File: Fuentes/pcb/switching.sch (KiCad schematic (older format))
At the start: 25 parts, among them P1 Vcc, P2 V-switching, P3 V+switching, P4 gnd_switching, P5 Gnd_primario, Q1 MOS_N

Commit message: placa conmutada algunas  pistas
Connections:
- net GND: now also C3.2, C4.1, P4.1 (W), R9.2, nucleo1.4 (GND_Secundario), nucleo1.5 (GND_secundario_2)
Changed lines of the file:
@@
-EESchema Schematic File Version 2  date mar 26 jun 2012 23:30:51 ART
+EESchema Schematic File Version 2  date jue 28 jun 2012 01:18:07 ART
 LIBS:power
 LIBS:device
@@
 Sheet 1 1
 Title ""
-Date "27 jun 2012"
+Date "28 jun 2012"
 Rev ""
 Comp ""
@@
 Comment4 ""
 $EndDescr
-Connection ~ 5400 4650
-Connection ~ 6950 2400
+Connection ~ 8850 2400
+Connection ~ 5600 4650
 Wire Wire Line
-	6950 2450 6950 2300
+	8850 4650 5300 4650
 Wire Wire Line
-	1400 4100 1250 4100
+	8850 4650 8850 2400
+Connection ~ 1500 4100
 Wire Wire Line
-	1300 4100 1500 4100
-Connection ~ 4800 4150
+	4800 4900 4800 4150
+Connection ~ 5550 3750
 Wire Wire Line
-	5000 4150 4800 4150
+	5550 2800 5550 3750
+Wire Wire Line
+	5300 4650 5300 4350
+Wire Wire Line
+	4800 4900 3900 4900
+Connection ~ 5550 2050
+Connection ~ 3900 5300
+Connection ~ 4650 4900
+Wire Wire Line
+	4650 4600 4650 5600
+Connection ~ 2100 4100
+Connection ~ 2100 5100
+Wire Wire Line
+	2100 5200 2100 4700
+Wire Wire Line
+	2100 5200 1900 5200
+Wire Wire Line
+	2600 4500 1750 4500
+Connection ~ 1250 4500
+Wire Wire Line
+	1250 4750 1250 4100
+Connection ~ 1750 4500
+Wire Wire Line
+	1750 4500 1750 4750
+Wire Wire Line
+	1750 4750 1700 4750
+Connection ~ 1400 4100
+Connection ~ 2100 4900
+Wire Wire Line
+	2100 5100 2600 5100
+Connection ~ 2450 4100
+Wire Wire Line
+	2450 4100 2450 3200
+Wire Wire Line
+	2600 3900 2600 3550
+Wire Wire Line
+	2600 3550 10050 3550
+Wire Wire Line
+	3900 4300 4050 4300
+Connection ~ 4400 3950
+Wire Wire Line
+	4400 3950 4650 3950
+Wire Wire Line
+	4650 5600 2600 5600
+Wire Wire Line
+	2600 5600 2600 5300
+Connection ~ 4400 2050
+Wire Wire Line
+	4400 2050 4400 4000
+Connection ~ 9150 1900
+Connection ~ 9150 2400
+Connection ~ 3900 3550
+Wire Wire Line
+	10050 3550 10050 1900
+Wire Wire Line
+	10050 1900 9150 1900
+Wire Wire Line
+	3900 5400 3900 5100
+Wire Wire Line
+	6950 2400 9150 2400
+Wire Wire Line
+	7400 2350 7400 2450
+Connection ~ 7400 2400
+Wire Wire Line
+	7400 1950 7400 1900
+Connection ~ 7400 1900
+Wire Wire Line
+	7400 2850 7400 2900
+Connection ~ 7400 2900
+Wire Wire Line
+	8200 2900 7350 2900
+Wire Wire Line
+	8250 1900 7350 1900
+Wire Wire Line
+	9150 1400 8200 1400
+Wire Wire Line
+	8200 1400 8200 1900
+Connection ~ 8200 1900
+Wire Wire Line
+	3900 4700 4400 4700
+Wire Wire Line
+	4400 4700 4400 4500
+Wire Wire Line
+	3900 4100 4050 4100
+Wire Wire Line
+	4050 4100 4050 3200
+Wire Wire Line
+	4050 3200 2450 3200
+Wire Wire Line
+	2600 4100 2000 4100
+Wire Wire Line
+	3900 3900 3900 3550
+Wire Wire Line
+	2100 4700 2200 4700
+Wire Wire Line
+	4650 3950 4650 4100
+Wire Wire Line
+	1250 4750 1300 4750
+Connection ~ 1900 4500
+Wire Wire Line
+	1900 4700 1900 4500
+Wire Wire Line
+	2100 4100 2100 4300
+Connection ~ 4800 4900
+Wire Wire Line
+	5300 3950 5300 3750
+Wire Wire Line
+	5300 3750 5600 3750
 Wire Wire Line
 	5550 2050 4150 2050
 Wire Wire Line
-	5600 3750 5300 3750
+	4800 4150 5000 4150
+Connection ~ 4800 4150
 Wire Wire Line
-	5300 3750 5300 3950
-Connection ~ 4800 4900
+	1300 4100 1500 4100
 Wire Wire Line
-	2100 4100 2100 4300
+	1250 4100 1400 4100
 Wire Wire Line
-	1900 4700 1900 4500
-Connection ~ 1900 4500
-Wire Wire Line
-	1300 4750 1250 4750
-Wire Wire Line
-	4650 4100 4650 3950
-Wire Wire Line
-	2200 4700 2100 4700
-Wire Wire Line
-	3900 3900 3900 3550
-Wire Wire Line
-	2600 4100 2000 4100
-Wire Wire Line
-	4050 3200 2450 3200
-Wire Wire Line
-	4050 3200 4050 4100
-Wire Wire Line
-	4050 4100 3900 4100
-Wire Wire Line
-	4400 4500 4400 4700
-Wire Wire Line
-	4400 4700 3900 4700
-Connection ~ 8200 1900
-Wire Wire Line
-	8200 1900 8200 1400
-Wire Wire Line
-	8200 1400 9150 1400
-Wire Wire Line
-	8250 1900 7350 1900
-Wire Wire Line
-	8200 2900 7350 2900
-Connection ~ 7400 2900
-Wire Wire Line
-	7400 2850 7400 2900
-Connection ~ 7400 1900
-Wire Wire Line
-	7400 1950 7400 1900
-Connection ~ 7400 2400
-Wire Wire Line
-	7400 2350 7400 2450
-Wire Wire Line
-	6950 2400 9150 2400
-Wire Wire Line
-	3900 5400 3900 5100
-Wire Wire Line
-	9150 1900 10050 1900
-Wire Wire Line
-	10050 1900 10050 3550
-Connection ~ 3900 3550
-Connection ~ 9150 2400
-Connection ~ 9150 1900
-Wire Wire Line
-	4400 2050 4400 4000
-Connection ~ 4400 2050
-Wire Wire Line
-	2600 5300 2600 5600
-Wire Wire Line
-	2600 5600 4650 5600
-Wire Wire Line
-	4650 3950 4400 3950
-Connection ~ 4400 3950
-Wire Wire Line
-	3900 4300 4050 4300
-Wire Wire Line
-	10050 3550 2600 3550
-Wire Wire Line
-	2600 3550 2600 3900
-Wire Wire Line
-	2450 3200 2450 4100
-Connection ~ 2450 4100
-Wire Wire Line
-	2100 5100 2600 5100
-Connection ~ 2100 4900
-Connection ~ 1400 4100
-Wire Wire Line
-	1700 4750 1750 4750
-Wire Wire Line
-	1750 4750 1750 4500
-Connection ~ 1750 4500
-Wire Wire Line
-	1250 4750 1250 4100
-Connection ~ 1250 4500
-Wire Wire Line
-	1750 4500 2600 4500
-Wire Wire Line
-	1900 5200 2100 5200
-Wire Wire Line
-	2100 5200 2100 4700
-Connection ~ 2100 5100
-Connection ~ 2100 4100
-Wire Wire Line
-	4650 5600 4650 4600
-Connection ~ 4650 4900
-Connection ~ 3900 5300
-Connection ~ 5550 2050
-Wire Wire Line
-	3900 4900 4800 4900
-Wire Wire Line
-	5300 4350 5300 4650
-Wire Wire Line
-	5300 4650 5600 4650
-Wire Wire Line
-	5550 2800 5550 3750
-Connection ~ 5550 3750
-Wire Wire Line
-	4800 4900 4800 4150
-Connection ~ 1500 4100
+	6950 2450 6950 2300
+Connection ~ 6950 2400
+Connection ~ 5400 4650
 $Comp
 L CONNECTOR P5

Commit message: 
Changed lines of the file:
@@
-EESchema Schematic File Version 2  date jue 28 jun 2012 01:18:07 ART
+EESchema Schematic File Version 2  date 28/06/2012 03:58:31 p.m.
 LIBS:power
 LIBS:device
@@
 LIBS:nucleo
 LIBS:lm494
-LIBS:switching-cache
+LIBS:sonic
 EELAYER 25  0
 EELAYER END
@@
 Comment4 ""
 $EndDescr
+$Comp
+L LOGO #G1
+U 1 1 4FECA926
+P 6250 5100
+F 0 "#G1" H 6250 4837 60  0001 C CNN
+F 1 "LOGO" H 6250 5363 60  0001 C CNN
+	1    6250 5100
+	1    0    0    -1
+$EndComp
 Connection ~ 8850 2400
 Connection ~ 5600 4650

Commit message: nueva switching beta
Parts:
- added C6: C, symbol C
- added F1: RELE, symbol RELE
- added Q2: NPN, symbol NPN
- added R11, R12, R13: R, symbol R
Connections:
- net GND: now also C6.2, Q2.1 (E), R12.1
- net at P1.1 (W), R6.2, R7.1: now also F1.2 (bobina2), F1.3 (cm), R11.2; no longer nucleo1.1 (V+Primario)
- new net: F1.4 (nc), nucleo1.1 (V+Primario)
- new net: F1.1 (bobina1), R13.1
- new net: C6.1, Q2.2 (B), R11.1, R12.2
- new net: Q2.3 (C), R13.2
- no-connect marks 0 -> 1
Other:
- moved on the sheet: C1, C2, C3, C4, C5, D1, D2, P1, P2, P3, P4, P5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

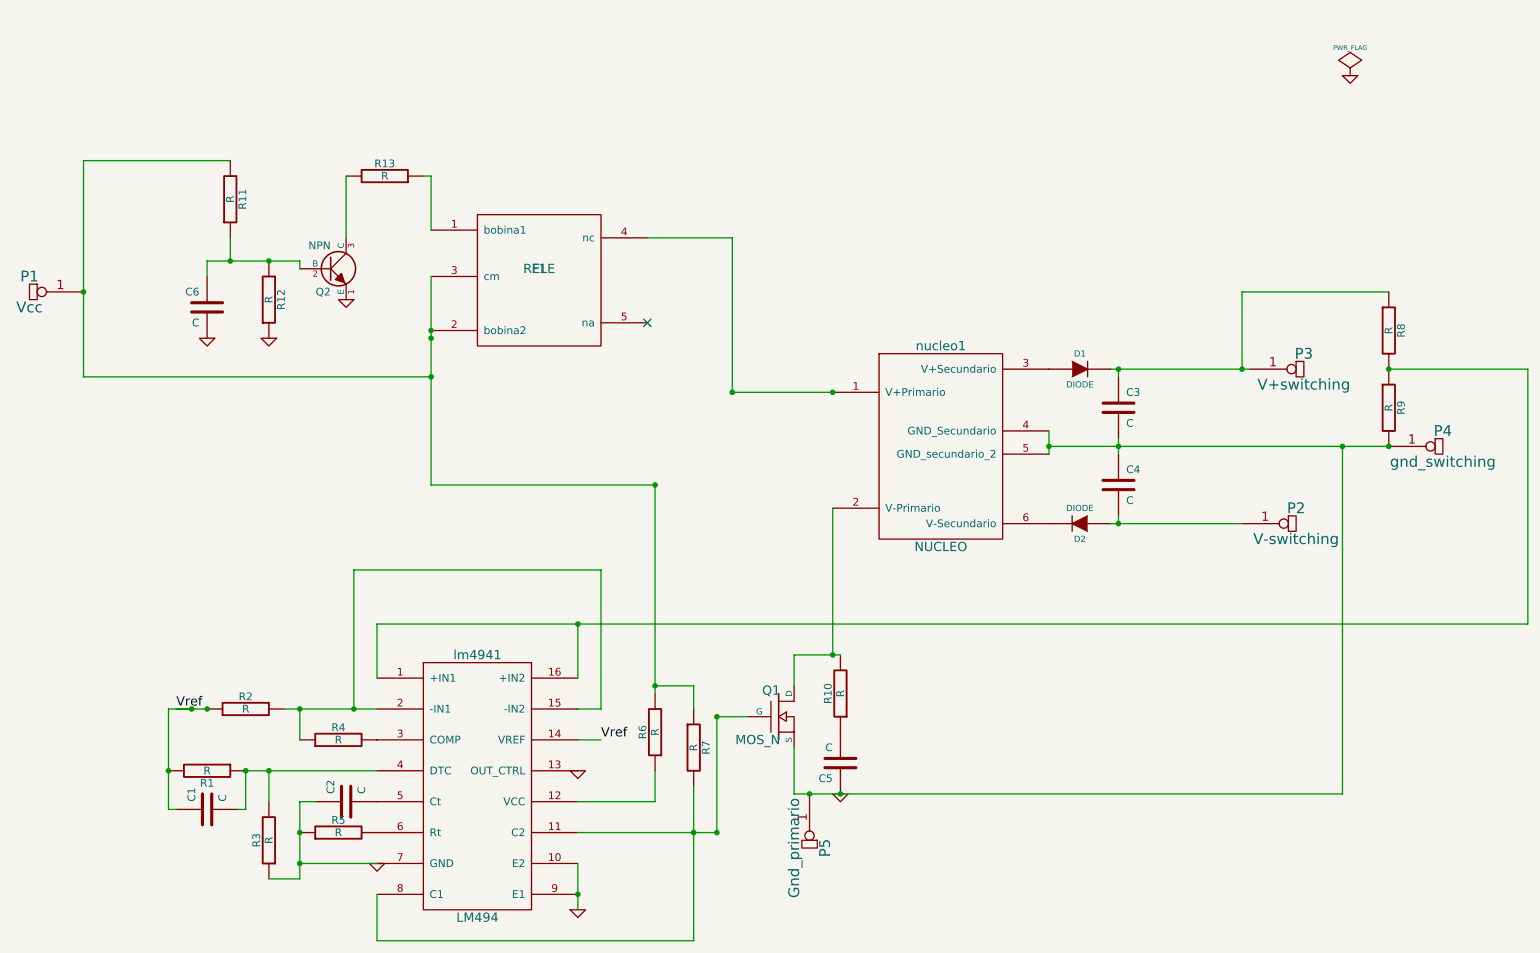
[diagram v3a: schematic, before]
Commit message: 
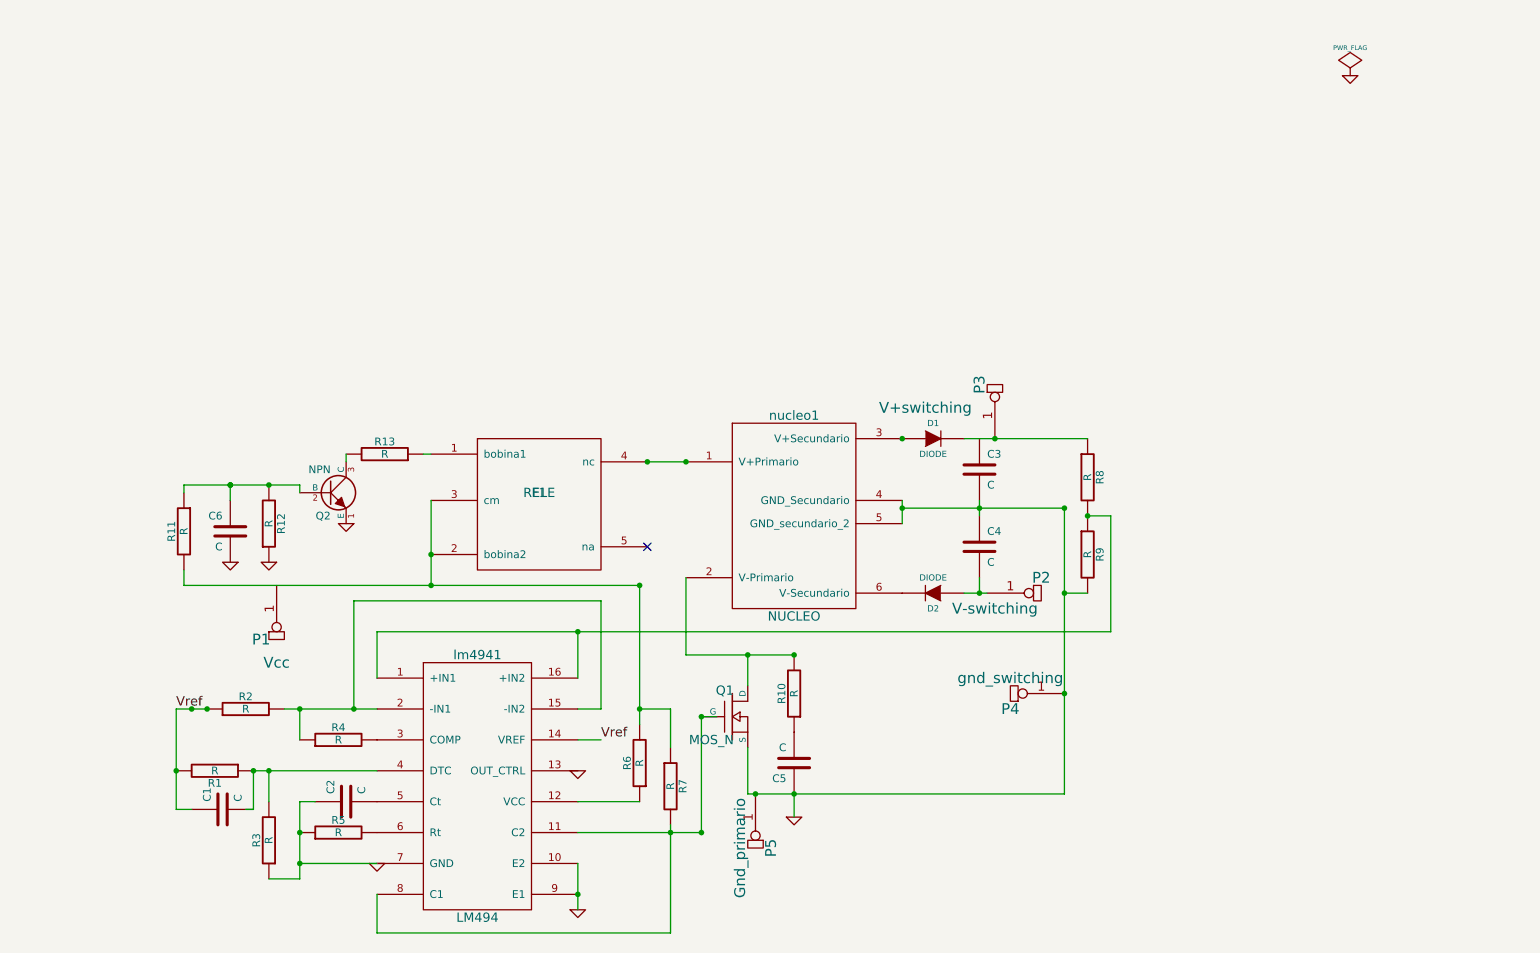
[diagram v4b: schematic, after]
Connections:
- wire segments 66 -> 58
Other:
- moved on the sheet: C1, C3, C4, C5, C6, D1, D2, F1, P1, P2, P3, P4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
